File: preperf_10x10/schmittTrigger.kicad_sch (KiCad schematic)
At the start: 6 parts, among them SW2 SW_Push, U12 74LS14

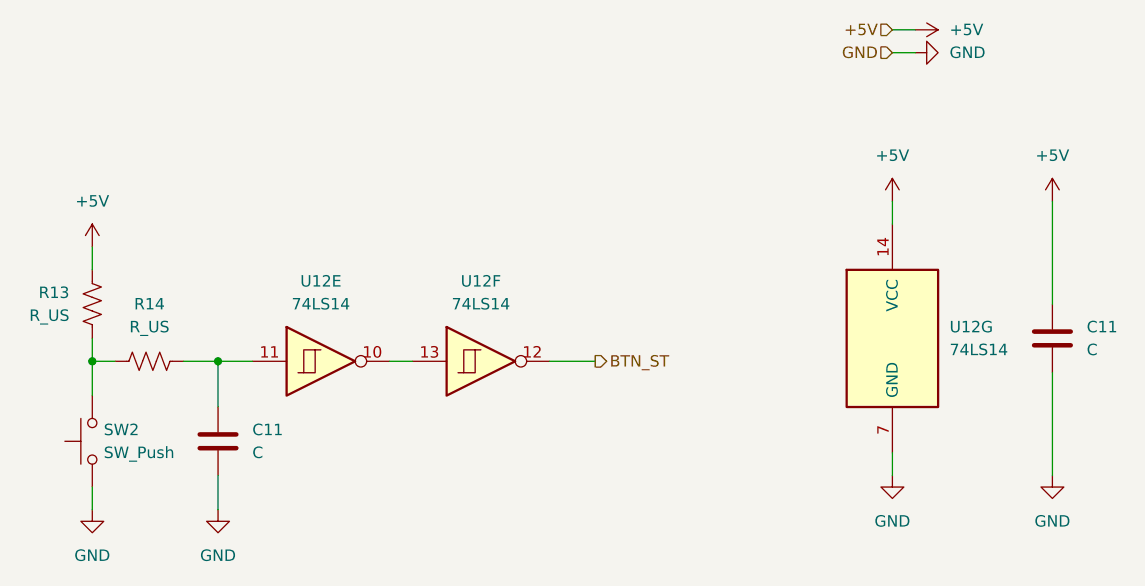
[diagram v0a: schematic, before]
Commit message: Added BCD Up counter with JK FF
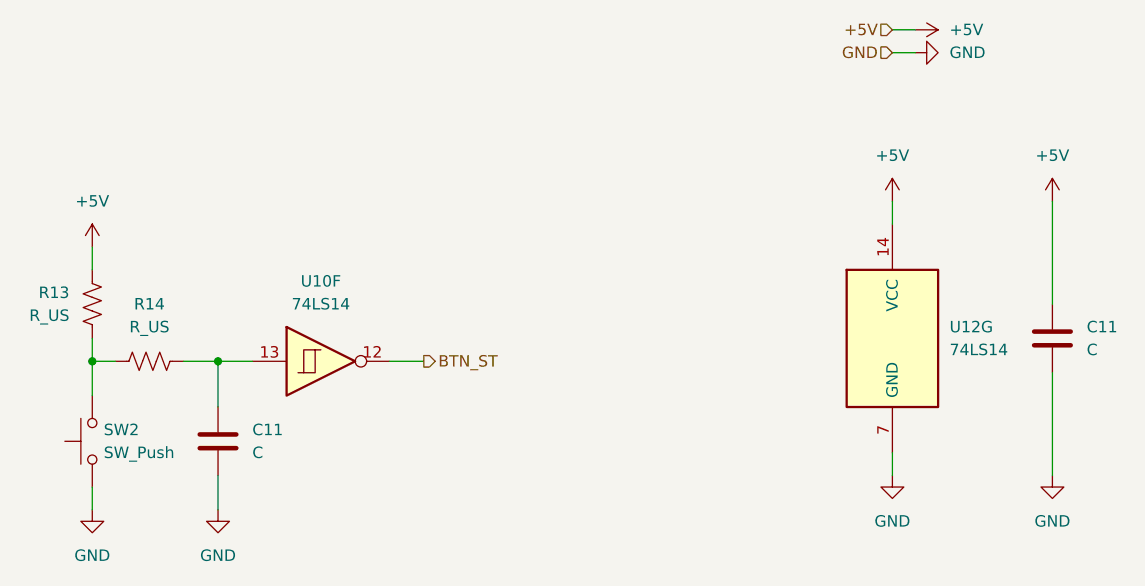
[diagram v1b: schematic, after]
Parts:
- removed unit 6 of U12
- removed unit 5 of U12
- added U10: 74LS14, Package_DIP:DIP-14_W7.62mm_Socket, symbol 74xx:74LS14
- C11: footprint Capacitor_THT:C_Disc_D5.0mm_W2.5mm_P2.50mm -> Capacitor_THT:C_Disc_D5.0mm_W2.5mm_P5.00mm
- R14: footprint Resistor_THT:R_Axial_DIN0207_L6.3mm_D2.5mm_P2.54mm_Vertical -> Resistor_THT:R_Axial_DIN0207_L6.3mm_D2.5mm_P7.62mm_Horizontal
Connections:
- net BTN_ST: now also U10.12
- net at C11.1, R14.2: now also U10.13

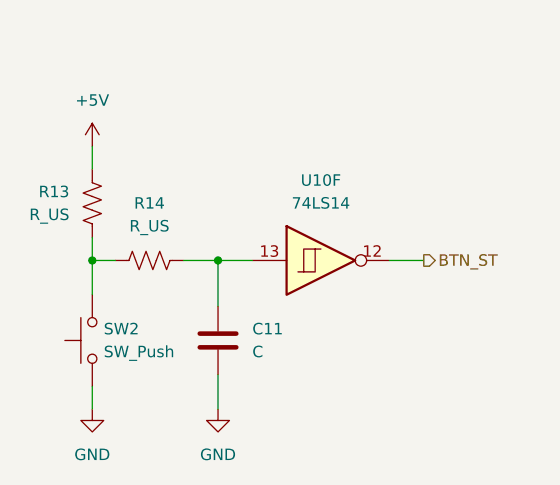
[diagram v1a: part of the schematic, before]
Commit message: Added BCD Counter UP (FF JK based)  and Power-On-Reset
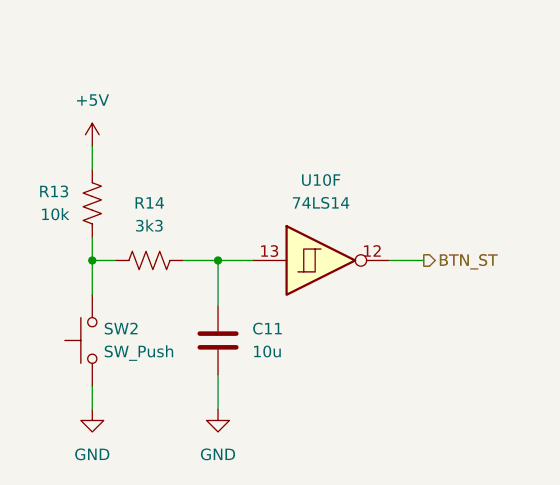
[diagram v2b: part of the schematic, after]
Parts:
- C11: value C -> 10u
- R13: value R_US -> 10k
- R14: value R_US -> 3k3
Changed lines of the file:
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@@
       (effects (font (size 1.27 1.27)) (justify right))
     )
-    (property "Value" "R_US" (at 41.91 63.5 0)
+    (property "Value" "10k" (at 41.91 63.5 0)
       (effects (font (size 1.27 1.27)) (justify right))
     )
@@
       (effects (font (size 1.27 1.27)))
     )
-    (property "Value" "R_US" (at 50.8 64.77 90)
+    (property "Value" "3k3" (at 50.8 64.77 90)
       (effects (font (size 1.27 1.27)))
     )
@@
       (effects (font (size 1.27 1.27)) (justify left))
     )
-    (property "Value" "C" (at 62.23 78.74 0)
-      (effects (font (size 1.27 1.27)) (justify left))
-    )
+    (property "Value" "10u" (at 62.23 78.74 0)
+      (effects (font (size 1.27 1.27)) (justify left))
+    )

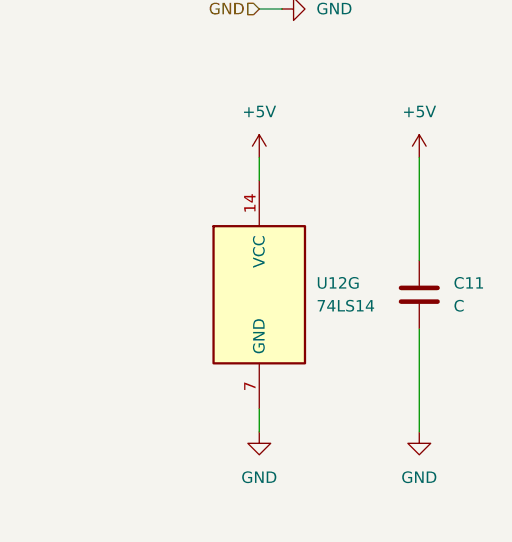
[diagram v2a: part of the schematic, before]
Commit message: [ADD] Digital Logic Design project (FIUBA): PCB implementation of schmitt triggers, logic functions, counters, state machines, and logic probes
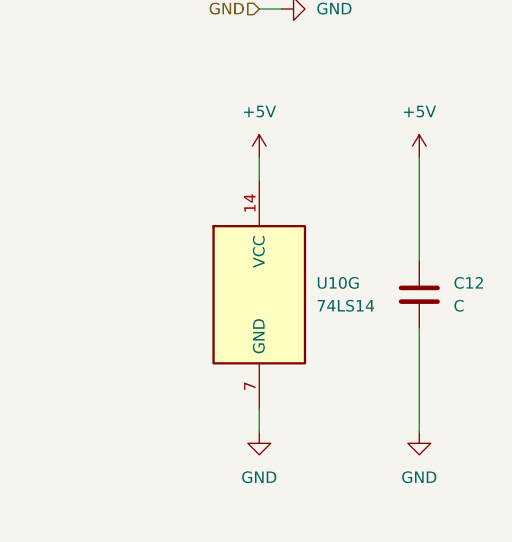
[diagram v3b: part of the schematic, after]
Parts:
- renumbered C11 to C12, U12 to U10
